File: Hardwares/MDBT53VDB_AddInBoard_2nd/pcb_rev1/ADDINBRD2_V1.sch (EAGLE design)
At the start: 17 parts, among them Q1 DMP2035UFDF-7, Q2 BC817-40QA, SW1 SKRPACE010, U1 SN74AHC1G00DRLR, U2 REF3325AIRSER, U3 MCP6232T-E/MNY

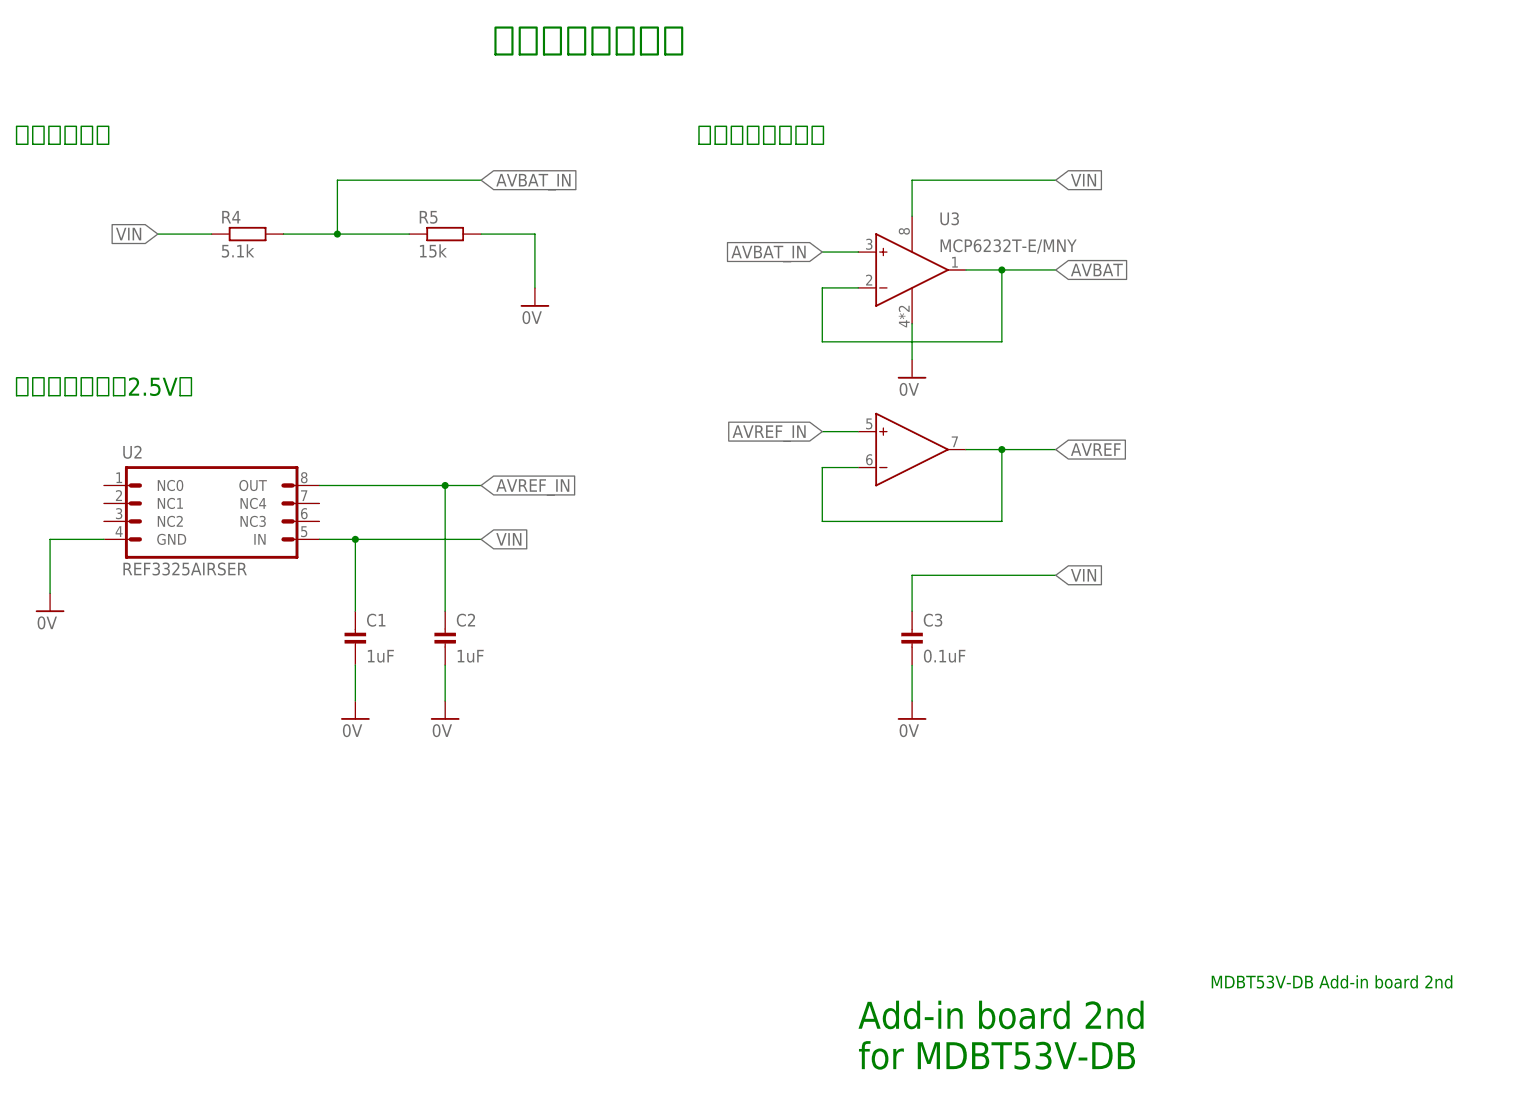
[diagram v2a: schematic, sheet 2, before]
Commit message: 回路図を修正
・電圧測定用の外部接続用端子を追加
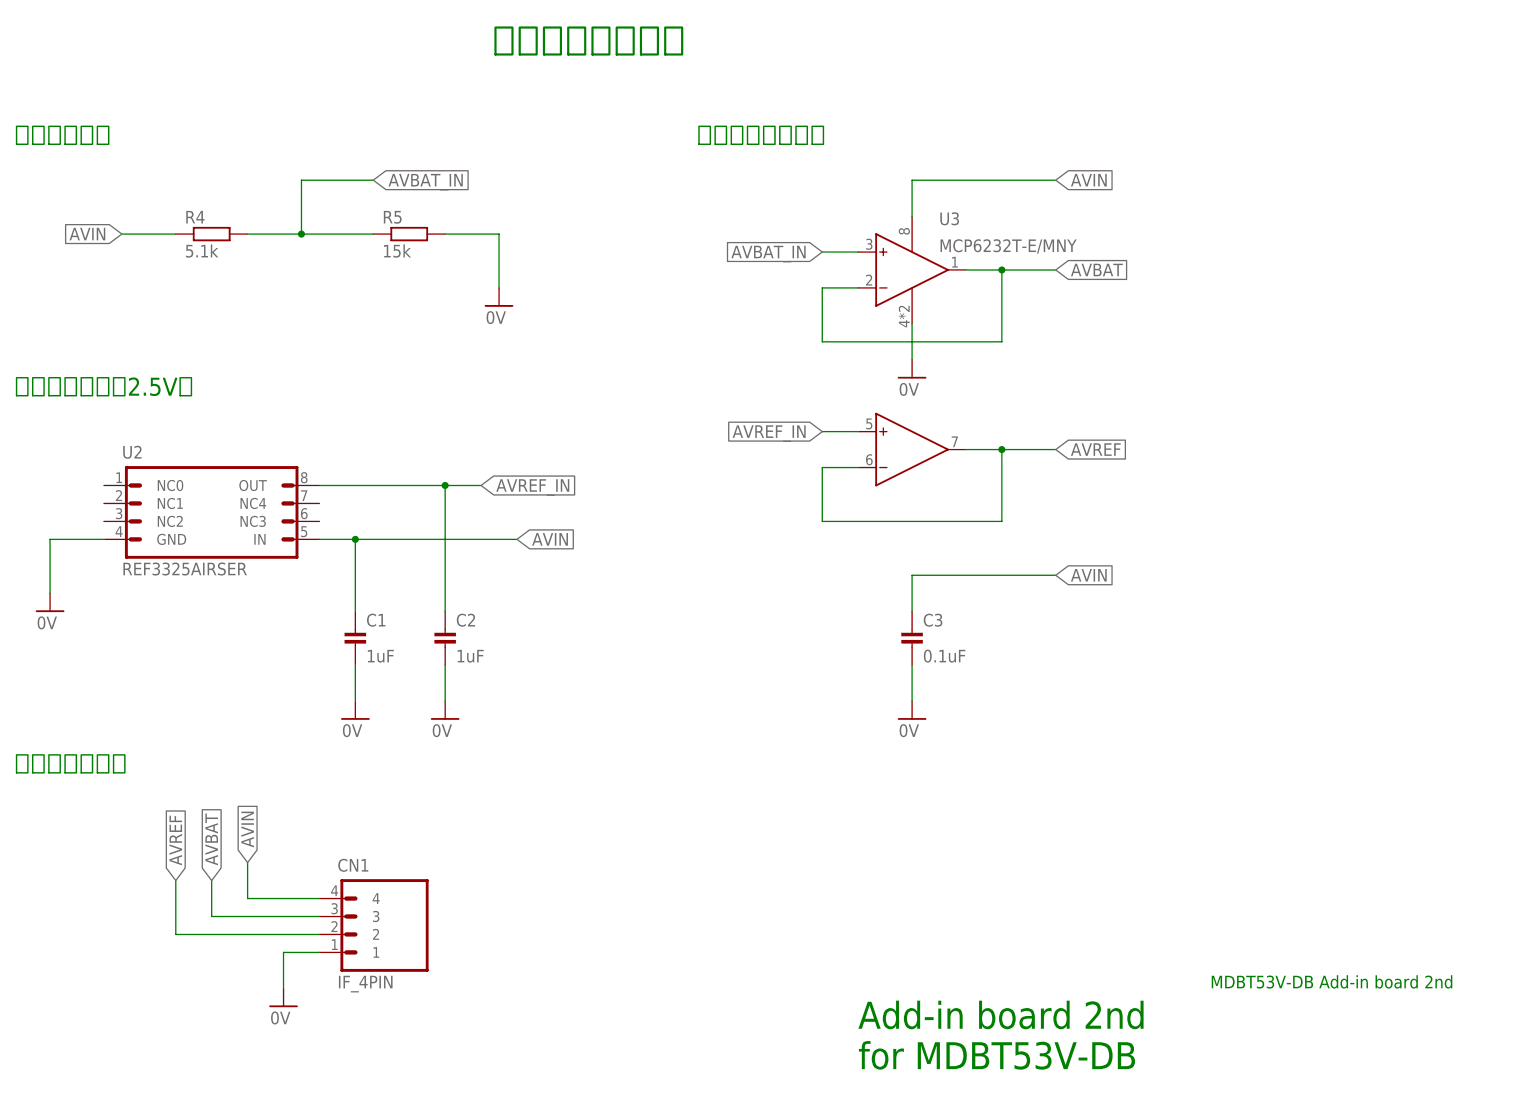
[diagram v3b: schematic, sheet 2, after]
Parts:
- added CN1: IF_4PIN, Connectors:IF_4PIN
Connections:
- new net AVIN: C1.1, C3.1, CN1.4, R4.1, U2.IN, U3.VDD
- net 0V: now also CN1.1
- net AVBAT: now also CN1.3
- net AVREF: now also CN1.2
- net VIN: no longer C1.1, C3.1, R4.1, U2.IN, U3.VDD
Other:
- note added: "外部接続用端子"
- moved on the sheet: R4, R5
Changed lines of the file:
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@@
 <part name="GND9" library="Supply" deviceset="0V" device=""/>
 <part name="GND11" library="Supply" deviceset="0V" device=""/>
+<part name="CN1" library="Connectors" deviceset="IF_4PIN" device=""/>
+<part name="GND10" library="Supply" deviceset="0V" device=""/>
 </parts>
 <sheets>
@@
 <text x="48.26" y="106.68" size="2.54" layer="91" align="top-left">基準電圧生成（2.5V）</text>
 <text x="144.78" y="142.24" size="2.54" layer="91" align="top-left">電圧入力バッファ</text>
+<text x="48.26" y="53.34" size="2.54" layer="91" align="top-left">外部接続用端子</text>
 </plain>
 <instances>
 <instance part="FRAME2" gate="G$1" x="0" y="0"/>
 <instance part="U2" gate="G$1" x="76.2" y="86.36"/>
-<instance part="GND5" gate="1" x="121.92" y="116.84"/>
+<instance part="GND5" gate="1" x="116.84" y="116.84"/>
 <instance part="GND6" gate="1" x="53.34" y="73.66"/>
 <instance part="GND7" gate="1" x="96.52" y="58.42"/>
@@
 <instance part="C1" gate="G$1" x="96.52" y="71.12"/>
 <instance part="C2" gate="G$1" x="109.22" y="71.12"/>
-<instance part="R4" gate="G$1" x="81.28" y="127"/>
-<instance part="R5" gate="G$1" x="109.22" y="127"/>
+<instance part="R4" gate="G$1" x="76.2" y="127"/>
+<instance part="R5" gate="G$1" x="104.14" y="127"/>
 <instance part="C3" gate="G$1" x="175.26" y="71.12"/>
 <instance part="U3" gate="G$1" x="170.18" y="109.22"/>
 <instance part="GND9" gate="1" x="175.26" y="106.68"/>
 <instance part="GND11" gate="1" x="175.26" y="58.42"/>
+<instance part="CN1" gate="G$1" x="91.44" y="33.02"/>
+<instance part="GND10" gate="1" x="86.36" y="17.78"/>
 </instances>
 <busses>
 </busses>
 <nets>
-<net name="VIN" class="0">
-<segment>
-<wire x1="76.2" y1="127" x2="68.58" y2="127" width="0.1524" layer="91"/>
-<label x="68.58" y="127" size="1.778" layer="95" rot="R180" xref="yes"/>
-<pinref part="R4" gate="G$1" pin="1"/>
-</segment>
-<segment>
-<pinref part="U2" gate="G$1" pin="IN"/>
-<wire x1="91.44" y1="83.82" x2="96.52" y2="83.82" width="0.1524" layer="91"/>
-<label x="114.3" y="83.82" size="1.778" layer="95" xref="yes"/>
-<wire x1="96.52" y1="83.82" x2="114.3" y2="83.82" width="0.1524" layer="91"/>
-<junction x="96.52" y="83.82"/>
-<pinref part="C1" gate="G$1" pin="1"/>
-<wire x1="96.52" y1="83.82" x2="96.52" y2="73.66" width="0.1524" layer="91"/>
-</segment>
-<segment>
-<pinref part="U3" gate="G$1" pin="VDD"/>
-<wire x1="175.26" y1="129.54" x2="175.26" y2="134.62" width="0.1524" layer="91"/>
-<wire x1="175.26" y1="134.62" x2="195.58" y2="134.62" width="0.1524" layer="91"/>
-<label x="195.58" y="134.62" size="1.778" layer="95" xref="yes"/>
-</segment>
-<segment>
-<pinref part="C3" gate="G$1" pin="1"/>
-<wire x1="175.26" y1="73.66" x2="175.26" y2="78.74" width="0.1524" layer="91"/>
-<wire x1="175.26" y1="78.74" x2="195.58" y2="78.74" width="0.1524" layer="91"/>
-<label x="195.58" y="78.74" size="1.778" layer="95" xref="yes"/>
-</segment>
-</net>
 <net name="AVBAT_IN" class="0">
 <segment>
-<wire x1="86.36" y1="127" x2="93.98" y2="127" width="0.1524" layer="91"/>
-<wire x1="93.98" y1="127" x2="104.14" y2="127" width="0.1524" layer="91"/>
-<wire x1="93.98" y1="127" x2="93.98" y2="134.62" width="0.1524" layer="91"/>
-<wire x1="93.98" y1="134.62" x2="114.3" y2="134.62" width="0.1524" layer="91"/>
-<junction x="93.98" y="127"/>
-<label x="114.3" y="134.62" size="1.778" layer="95" xref="yes"/>
+<wire x1="81.28" y1="127" x2="88.9" y2="127" width="0.1524" layer="91"/>
+<wire x1="88.9" y1="127" x2="99.06" y2="127" width="0.1524" layer="91"/>
+<wire x1="88.9" y1="127" x2="88.9" y2="134.62" width="0.1524" layer="91"/>
+<wire x1="88.9" y1="134.62" x2="99.06" y2="134.62" width="0.1524" layer="91"/>
+<junction x="88.9" y="127"/>
+<label x="99.06" y="134.62" size="1.778" layer="95" xref="yes"/>
 <pinref part="R4" gate="G$1" pin="2"/>
 <pinref part="R5" gate="G$1" pin="1"/>
@@
 <segment>
 <pinref part="GND5" gate="1" pin="0V"/>
-<wire x1="114.3" y1="127" x2="121.92" y2="127" width="0.1524" layer="91"/>
-<wire x1="121.92" y1="127" x2="121.92" y2="119.38" width="0.1524" layer="91"/>
+<wire x1="109.22" y1="127" x2="116.84" y2="127" width="0.1524" layer="91"/>
+<wire x1="116.84" y1="127" x2="116.84" y2="119.38" width="0.1524" layer="91"/>
 <pinref part="R5" gate="G$1" pin="2"/>
 </segment>
@@
 <pinref part="C3" gate="G$1" pin="2"/>
 <wire x1="175.26" y1="60.96" x2="175.26" y2="66.04" width="0.1524" layer="91"/>
+</segment>
+<segment>
+<pinref part="CN1" gate="G$1" pin="1"/>
+<pinref part="GND10" gate="1" pin="0V"/>
+<wire x1="91.44" y1="25.4" x2="86.36" y2="25.4" width="0.1524" layer="91"/>
+<wire x1="86.36" y1="25.4" x2="86.36" y2="20.32" width="0.1524" layer="91"/>
 </segment>
 </net>
@@
 <wire x1="162.56" y1="119.38" x2="167.64" y2="119.38" width="0.1524" layer="91"/>
 </segment>
+<segment>
+<pinref part="CN1" gate="G$1" pin="3"/>
+<wire x1="91.44" y1="30.48" x2="76.2" y2="30.48" width="0.1524" layer="91"/>
+<wire x1="76.2" y1="30.48" x2="76.2" y2="35.56" width="0.1524" layer="91"/>
+<label x="76.2" y="35.56" size="1.778" layer="95" rot="R90" xref="yes"/>
+</segment>
 </net>
 <net name="AVREF" class="0">
@@
 <wire x1="162.56" y1="93.98" x2="167.64" y2="93.98" width="0.1524" layer="91"/>
 </segment>
-</net>
+<segment>
+<pinref part="CN1" gate="G$1" pin="2"/>
+<wire x1="91.44" y1="27.94" x2="71.12" y2="27.94" width="0.1524" layer="91"/>
+<wire x1="71.12" y1="27.94" x2="71.12" y2="35.56" width="0.1524" layer="91"/>
+<label x="71.12" y="35.56" size="1.778" layer="95" rot="R90" xref="yes"/>
+</segment>
+</net>
+<net name="AVIN" class="0">
+<segment>
+<pinref part="CN1" gate="G$1" pin="4"/>
+<wire x1="91.44" y1="33.02" x2="81.28" y2="33.02" width="0.1524" layer="91"/>
+<wire x1="81.28" y1="33.02" x2="81.28" y2="38.1" width="0.1524" layer="91"/>
+<label x="81.28" y="38.1" size="1.778" layer="95" rot="R90" xref="yes"/>
+</segment>
+<segment>
+<pinref part="R4" gate="G$1" pin="1"/>
+<wire x1="71.12" y1="127" x2="63.5" y2="127" width="0.1524" layer="91"/>
+<label x="63.5" y="127" size="1.778" layer="95" rot="R180" xref="yes"/>
+</segment>
+<segment>
+<pinref part="U2" gate="G$1" pin="IN"/>
+<wire x1="91.44" y1="83.82" x2="96.52" y2="83.82" width="0.1524" layer="91"/>
+<pinref part="C1" gate="G$1" pin="1"/>
+<wire x1="96.52" y1="83.82" x2="119.38" y2="83.82" width="0.1524" layer="91"/>
+<wire x1="96.52" y1="73.66" x2="96.52" y2="83.82" width="0.1524" layer="91"/>
+<label x="119.38" y="83.82" size="1.778" layer="95" xref="yes"/>
+<junction x="96.52" y="83.82"/>
+</segment>
+<segment>
+<pinref part="C3" gate="G$1" pin="1"/>
+<wire x1="175.26" y1="73.66" x2="175.26" y2="78.74" width="0.1524" layer="91"/>
+<wire x1="175.26" y1="78.74" x2="195.58" y2="78.74" width="0.1524" layer="91"/>
+<label x="195.58" y="78.74" size="1.778" layer="95" xref="yes"/>
+</segment>
+<segment>
+<pinref part="U3" gate="G$1" pin="VDD"/>
+<wire x1="175.26" y1="129.54" x2="175.26" y2="134.62" width="0.1524" layer="91"/>
+<wire x1="175.26" y1="134.62" x2="195.58" y2="134.62" width="0.1524" layer="91"/>
+<label x="195.58" y="134.62" size="1.778" layer="95" xref="yes"/>
+</segment>
+</net>

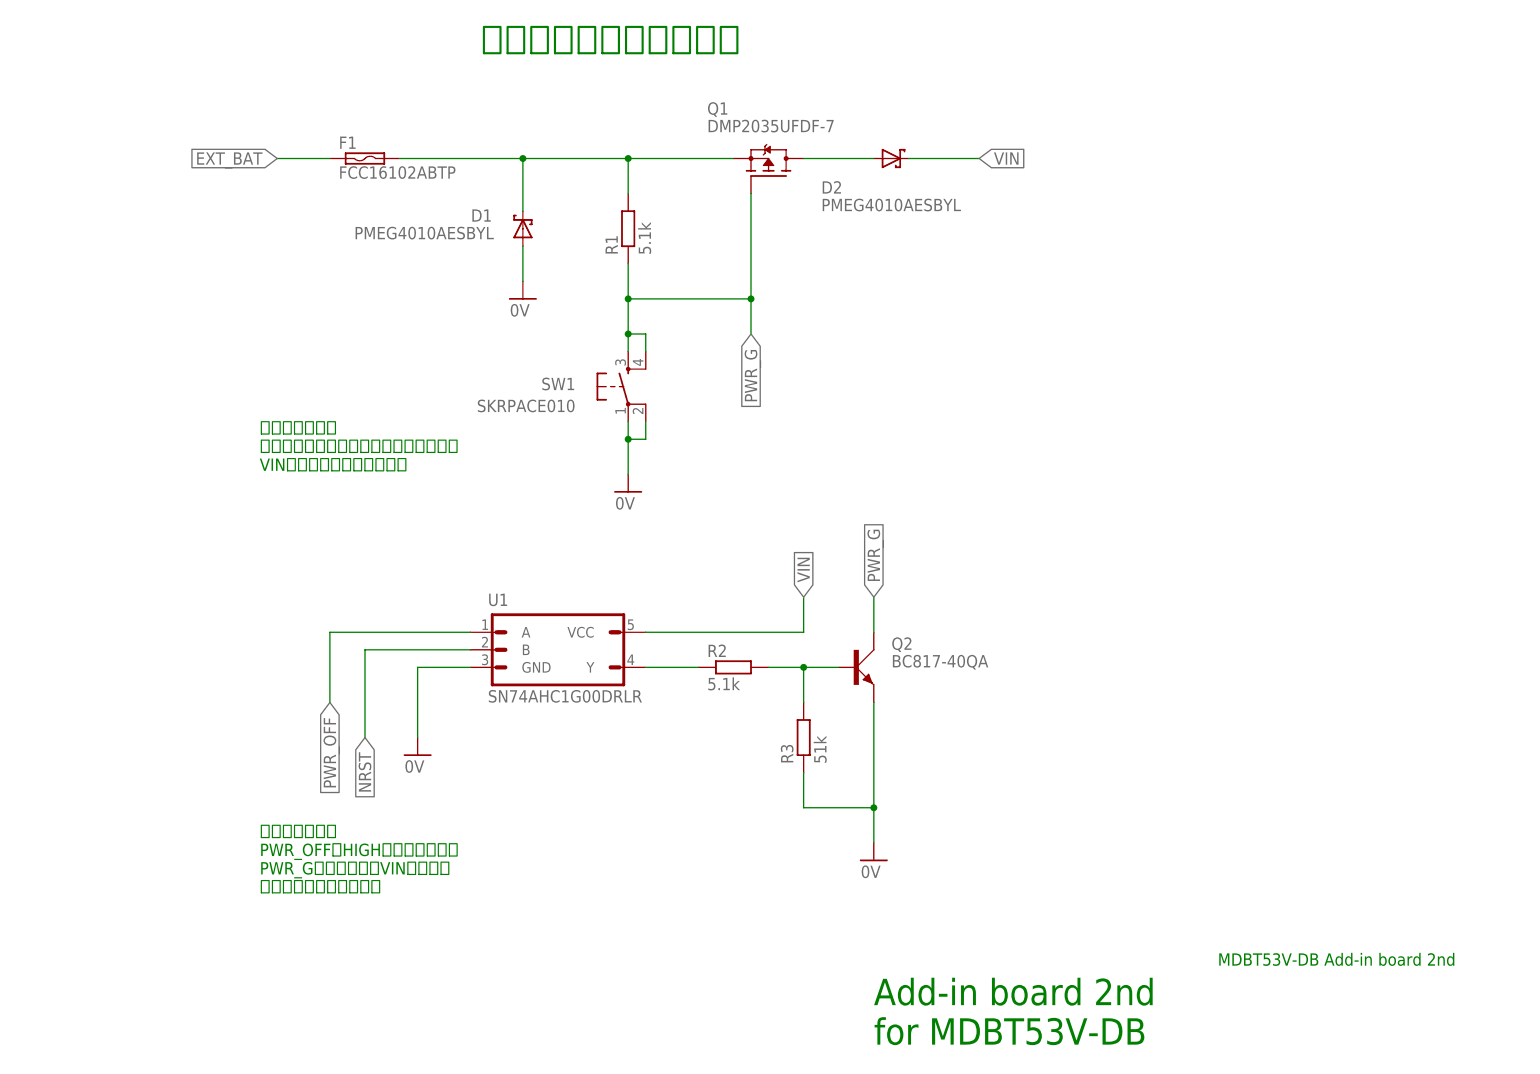
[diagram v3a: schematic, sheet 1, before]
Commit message: 回路図を修正
・外部接続用端子を設置
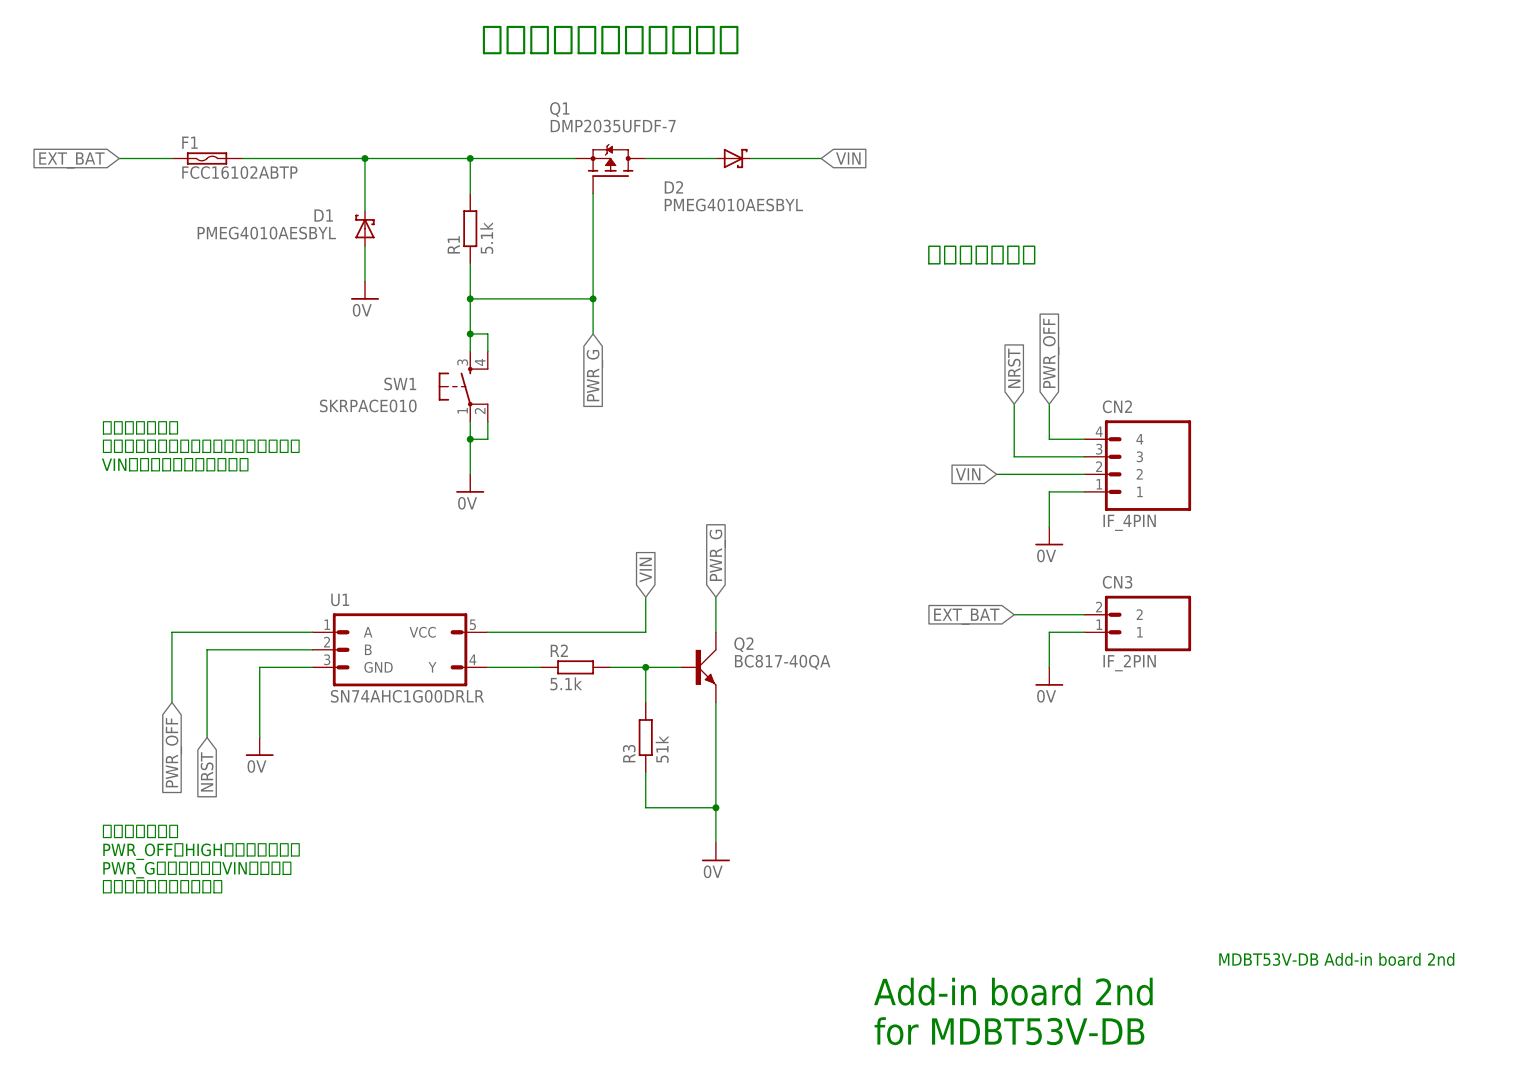
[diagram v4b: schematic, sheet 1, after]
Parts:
- added CN2: IF_4PIN, Connectors:IF_4PIN
- added CN3, CN4: IF_2PIN, Connectors:IF_2PIN
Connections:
- net 0V: now also CN2.1, CN3.1
- net AVIN: now also CN4.1
- net EXT_BAT: now also CN3.2
- net NRST: now also CN2.3
- net PWR_OFF: now also CN2.4
- net VIN: now also CN2.2, CN4.2
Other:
- moved on the sheet: CN1, D1, D2, F1, Q1, Q2, R1, R2, R3, R4, R5, SW1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
